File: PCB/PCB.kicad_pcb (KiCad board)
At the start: 2 copper layers, 208.3 x 169.5 mm, 308 parts, among them J55001 Debug, J60001 ALS, J60003 I2C, SW10001 SW_Push, SW11001 SW_Push, SW12001 SW_Push, SW13001 SW_Push, SW14001 SW_Push, SW17001 SW_Push, SW18001 SW_Push, SW19001 SW_Push, SW20001 SW_Push, SW2001 SW_Push, SW21001 SW_Push, SW22001 SW_Push, SW24001 SW_Push, SW25001 SW_Push, SW26001 SW_Push, SW27001 SW_Push, SW28001 SW_Push, SW30001 SW_Push, SW3001 SW_Push, SW31001 SW_Push, SW33001 SW_Push, SW34001 SW_Push, SW35001 SW_Push, SW36001 SW_Push, SW37001 SW_Push, SW38001 SW_Push, SW39001 SW_Push, SW40001 SW_Push, SW4001 SW_Push, SW44001 SW_Push, SW45001 SW_Push, SW46001 SW_Push, SW47001 SW_Push, SW48001 SW_Push, SW50001 SW_Push, SW5001 SW_Push, SW51001 SW_Push, SW53001 SW_Push, SW59001 SW_Push, SW60001 SW_Push, SW6001 SW_Push, SW61001 SW_Push, SW7001 SW_Push, SW8001 SW_Push, SW9001 SW_Push, U10001 SK6812MINI-E_C5149201, U11001 SK6812MINI-E_C5149201, U12001 SK6812MINI-E_C5149201, U13001 SK6812MINI-E_C5149201, U14001 SK6812MINI-E_C5149201, U17001 SK6812MINI-E_C5149201, U18001 SK6812MINI-E_C5149201, U19001 SK6812MINI-E_C5149201, U20001 SK6812MINI-E_C5149201, U2001 SK6812MINI-E_C5149201, U21001 SK6812MINI-E_C5149201, U22001 SK6812MINI-E_C5149201, U24001 SK6812MINI-E_C5149201, U25001 SK6812MINI-E_C5149201, U26001 SK6812MINI-E_C5149201, U27001 SK6812MINI-E_C5149201, U28001 SK6812MINI-E_C5149201, U30001 SK6812MINI-E_C5149201, U3001 SK6812MINI-E_C5149201, U31001 SK6812MINI-E_C5149201, U33001 SK6812MINI-E_C5149201, U34001 SK6812MINI-E_C5149201, U35001 SK6812MINI-E_C5149201, U36001 SK6812MINI-E_C5149201, U37001 SK6812MINI-E_C5149201, U38001 SK6812MINI-E_C5149201, U39001 SK6812MINI-E_C5149201, U40001 SK6812MINI-E_C5149201, U4001 SK6812MINI-E_C5149201, U44001 SK6812MINI-E_C5149201, U45001 SK6812MINI-E_C5149201, U46001 SK6812MINI-E_C5149201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

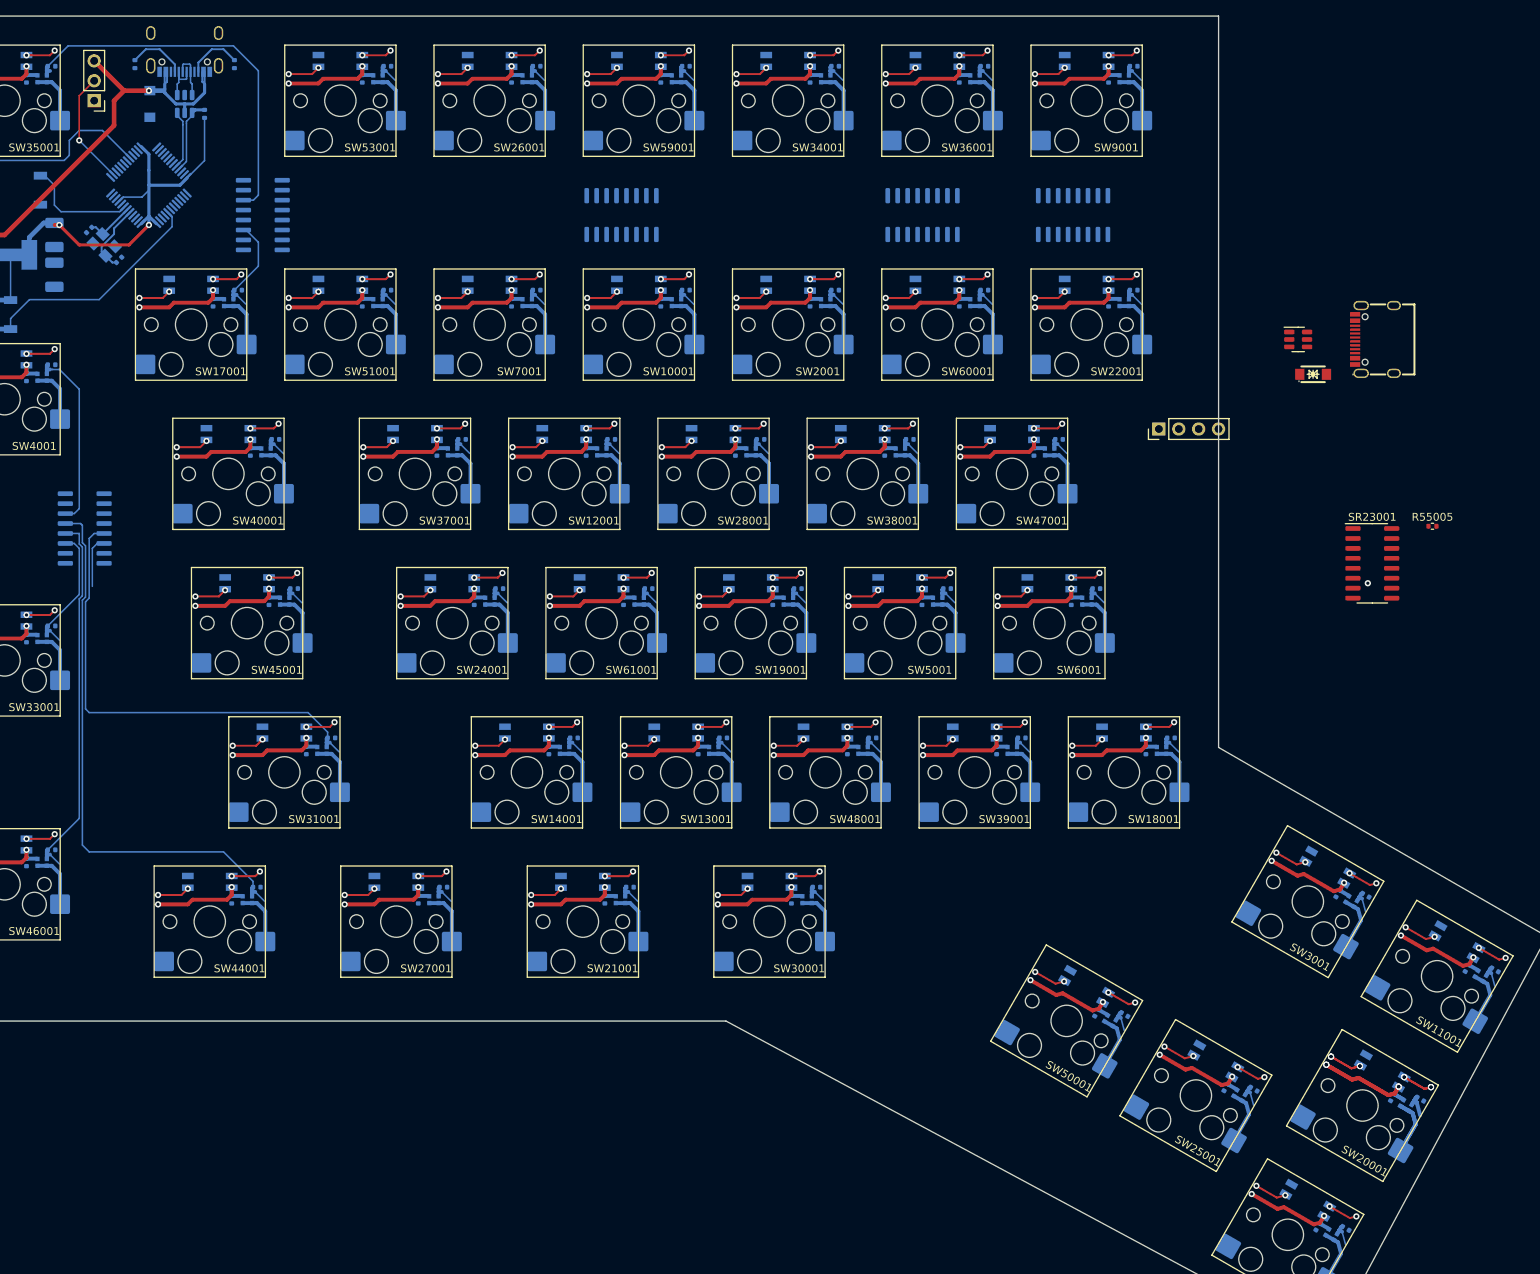
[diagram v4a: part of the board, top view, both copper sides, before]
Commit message: Updated schematics for KiCAD 8
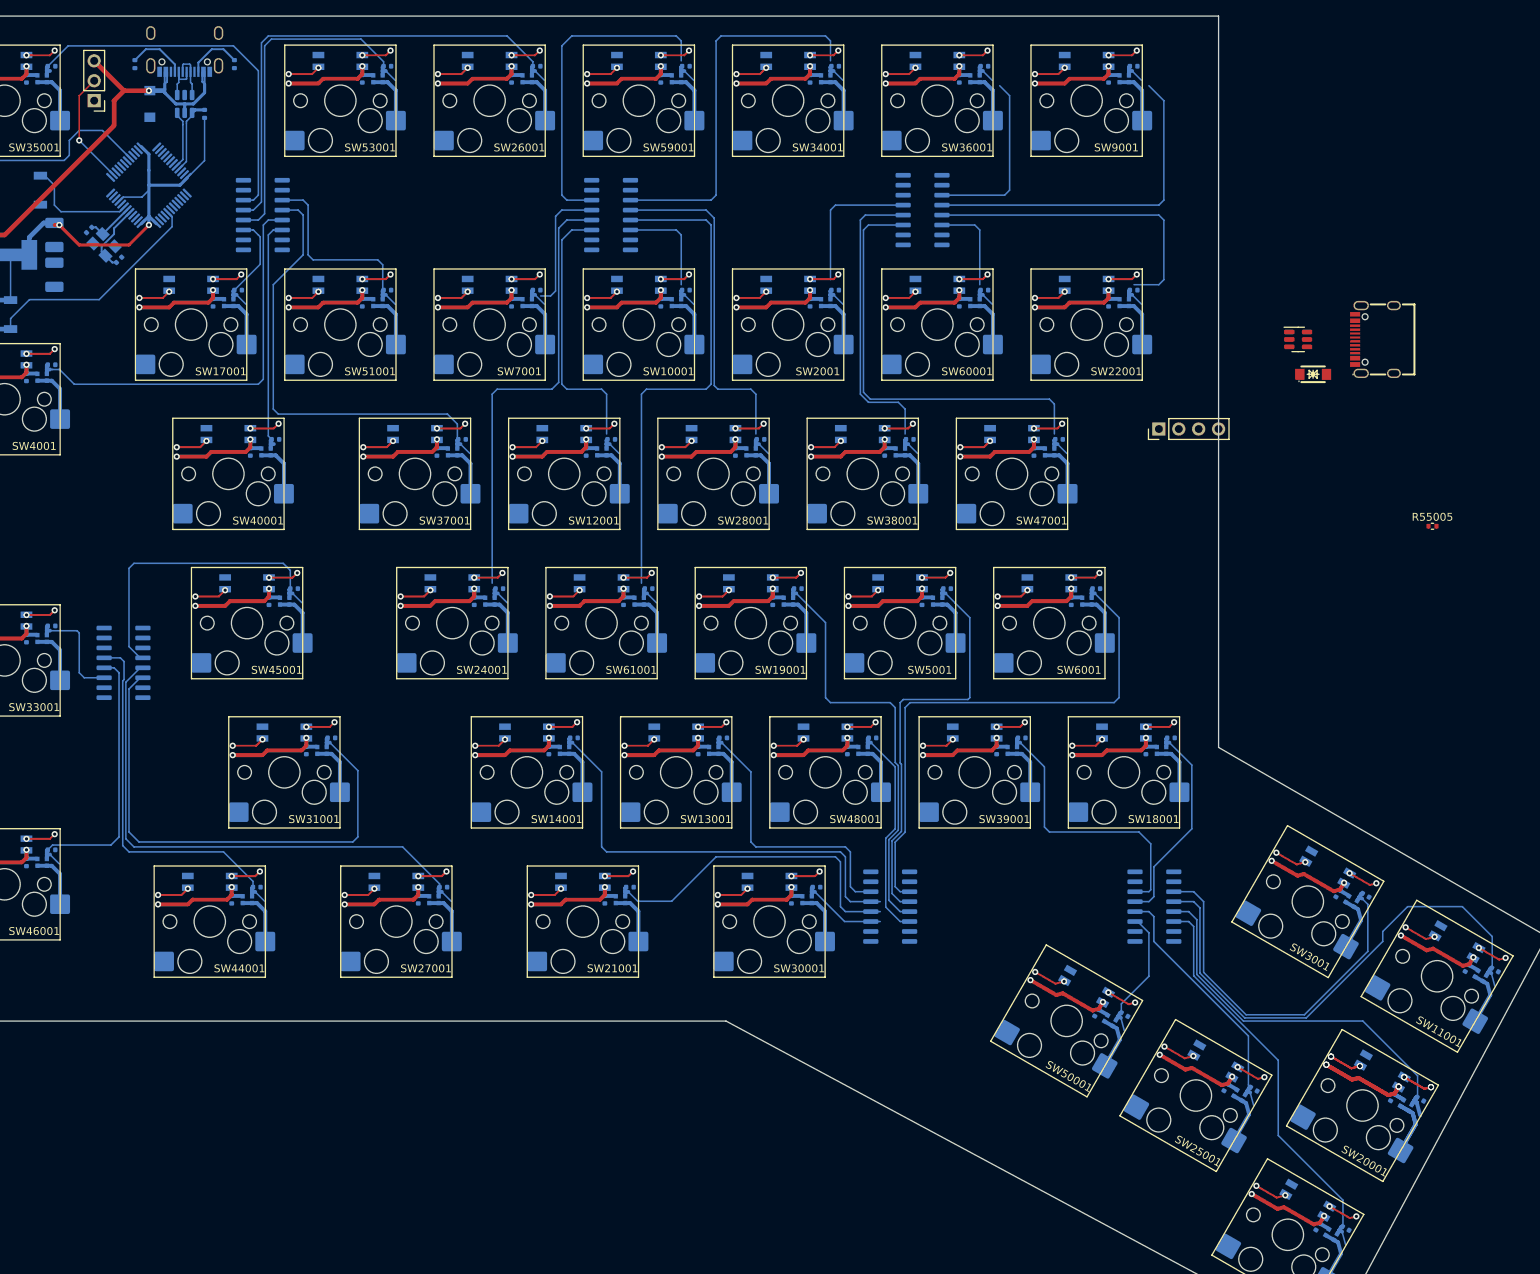
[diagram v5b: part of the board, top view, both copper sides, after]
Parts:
- SR23001: moved to B.Cu
- moved SR32001 91.3 mm to (143.5, 134.0), turned to 180 degrees
- moved SR23001 51.9 mm to (177.2, 134.0), turned to 180 degrees
- moved SR54001 17.8 mm to (45.7, 102.9)
- moved SR42001 1.33 mm to (107.9, 45.7), turned to 180 degrees
- moved SR16001 0.63 mm to (147.6, 45.1), turned to 180 degrees
- turned SR15001 to 180 degrees
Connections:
- CS35001 pad 2: /Left Half/8-Key Module2/SWIN1 -> /Left Half/Key Unit31/SwitchOutput
- RB35001 pad 1: /Left Half/8-Key Module2/SWIN1 -> /Left Half/Key Unit31/SwitchOutput
- SR15001 pad 11: /Left Half/8-Key Module2/SWIN8 -> /Left Half/Key Unit15/SwitchOutput
- SR15001 pad 12: /Left Half/8-Key Module2/SWIN7 -> /Left Half/Key Unit45/SwitchOutput
- SR15001 pad 13: /Left Half/8-Key Module2/SWIN6 -> /Left Half/Key Unit21/SwitchOutput
- SR15001 pad 14: /Left Half/8-Key Module2/SWIN5 -> /Left Half/Key Unit31/SwitchOutput
- SR15001 pad 3: /Left Half/Key Unit15/SwitchOutput -> /Left Half/Key Unit47/SwitchOutput
- SR15001 pad 4: /Left Half/8-Key Module2/SWIN3 -> /Left Half/Key Unit32/SwitchOutput
- SR15001 pad 5: /Left Half/8-Key Module2/SWIN2 -> /Left Half/Key Unit3/SwitchOutput
- SR15001 pad 6: /Left Half/8-Key Module2/SWIN1 -> /Left Half/Key Unit42/SwitchOutput
- SR23001 pad 11: /Left Half/8-Key Module5/SWIN8 -> /Left Half/Key Unit40/SwitchOutput
- SR23001 pad 12: /Left Half/8-Key Module5/SWIN7 -> /Left Half/Key Unit27/SwitchOutput
- SR23001 pad 13: /Left Half/8-Key Module5/SWIN6 -> /Left Half/Key Unit11/SwitchOutput
- SR23001 pad 14: /Left Half/8-Key Module5/SWIN5 -> /Left Half/Key Unit37/SwitchOutput
- SR23001 pad 3: /Left Half/8-Key Module5/SWIN4 -> /Left Half/Key Unit7/SwitchOutput
- SR23001 pad 4: /Left Half/8-Key Module5/SWIN3 -> /Left Half/Key Unit20/SwitchOutput
- SR23001 pad 5: /Left Half/8-Key Module5/SWIN2 -> /Left Half/Key Unit24/SwitchOutput
- SR23001 pad 6: /Left Half/8-Key Module5/SWIN1 -> /Left Half/Key Unit2/SwitchOutput
- SR32001 pad 11: /Left Half/8-Key Module4/SWIN8 -> /Left Half/Key Unit30/SwitchOutput
- SR32001 pad 12: /Left Half/8-Key Module4/SWIN7 -> /Left Half/Key Unit23/SwitchOutput
- SR32001 pad 13: /Left Half/8-Key Module4/SWIN6 -> /Left Half/Key Unit14/SwitchOutput
- SR32001 pad 14: /Left Half/8-Key Module4/SWIN5 -> /Left Half/Key Unit18/SwitchOutput
- SR32001 pad 3: /Left Half/8-Key Module4/SWIN4 -> /Left Half/Key Unit5/SwitchOutput
- SR32001 pad 4: /Left Half/8-Key Module4/SWIN3 -> /Left Half/Key Unit1/SwitchOutput
- SR32001 pad 5: /Left Half/8-Key Module4/SWIN2 -> /Left Half/Key Unit17/SwitchOutput
- SR32001 pad 6: /Left Half/8-Key Module4/SWIN1 -> /Left Half/Key Unit41/SwitchOutput
- SR54001 pad 14: /Left Half/Key Unit3/SwitchOutput -> (no net)
- SR54001 pad 3: /Left Half/8-Key Module/SWIN4 -> (no net)
- SR54001 pad 4: /Left Half/8-Key Module/SWIN3 -> /Left Half/Key Unit44/SwitchOutput
- SR54001 pad 5: /Left Half/Key Unit34/SwitchOutput -> /Left Half/Key Unit26/SwitchOutput
- SR54001 pad 6: /Left Half/8-Key Module/SWIN1 -> /Left Half/Key Unit34/SwitchOutput
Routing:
- net /Left Half/Key Unit5/SwitchOutput: track 3.31 -> 69.5 mm
- net /Left Half/Key Unit26/SwitchOutput: track 3.31 -> 69.1 mm
- net /Left Half/8-Key Module1/SWIN2: track 0.00 -> 64.4 mm
- net /Left Half/Key Unit20/SwitchOutput: track 3.31 -> 67.2 mm
- net /Left Half/Key Unit21/SwitchOutput: track 3.31 -> 63.9 mm
- net /Left Half/8-Key Module1/SWIN7: track 0.00 -> 57.6 mm
- net /Left Half/Key Unit32/SwitchOutput: track 3.31 -> 58.9 mm
- net /Left Half/8-Key Module3/SWIN8: track 0.00 -> 54.8 mm
- net /Left Half/Key Unit14/SwitchOutput: track 3.31 -> 57.9 mm
- net /Left Half/Key Unit17/SwitchOutput: track 3.31 -> 54.4 mm
- net /Left Half/Key Unit1/SwitchOutput: track 3.31 -> 53.0 mm
- net /Left Half/Key Unit2/SwitchOutput: track 3.31 -> 52.3 mm
- net /Left Half/Key Unit31/SwitchOutput: track 0.00 -> 48.9 mm
- net /Left Half/8-Key Module2/SWIN1: track 48.9 -> 0.00 mm
- net /Left Half/8-Key Module1/SWIN4: track 0.00 -> 48.5 mm
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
